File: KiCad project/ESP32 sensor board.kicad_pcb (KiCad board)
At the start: 4 copper layers, 89.5 x 52.8 mm, 85 parts, among them J1 USB_C_Receptacle, J2 JST_2mm_LiPo, J3 GSD090012SEU, J4 B4B-XH-AM, J6 Conn_01x05, Q1 TEMT6000X01, Q2 BC817, Q3 BC817, SW1 1101NE, SW2 1101NE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

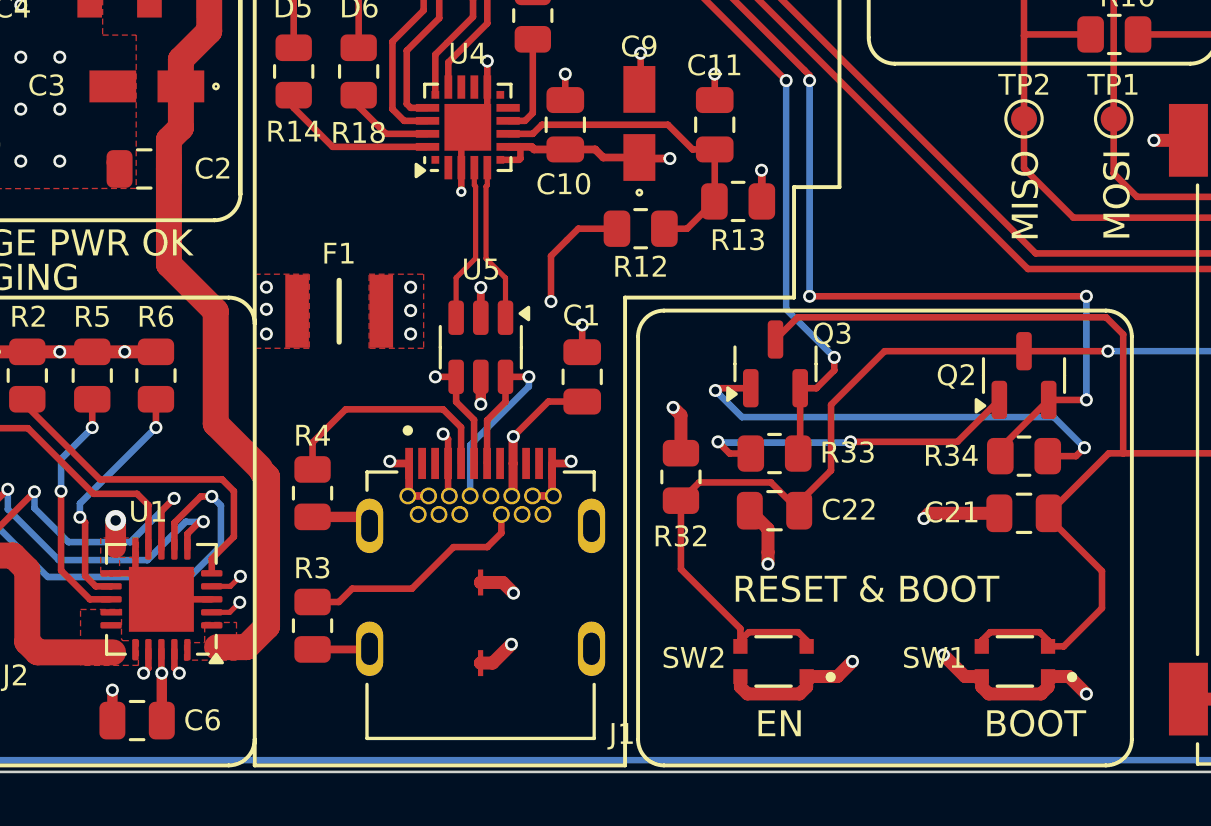
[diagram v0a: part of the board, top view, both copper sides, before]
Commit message: Additional checks completed, and Gerbers exported for HQDFM. Looking good for manufacturing.
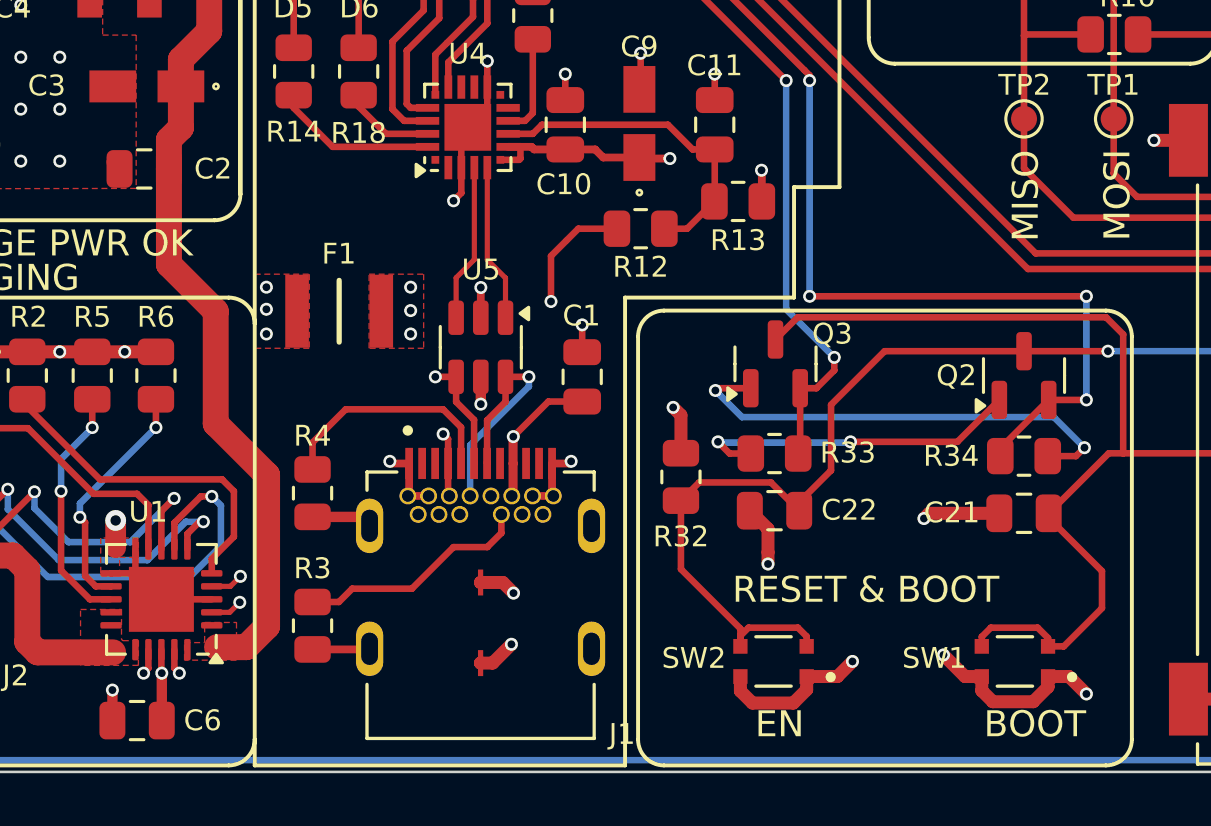
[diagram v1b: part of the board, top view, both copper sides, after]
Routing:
- net GND: track 120.6 -> 121.8 mm

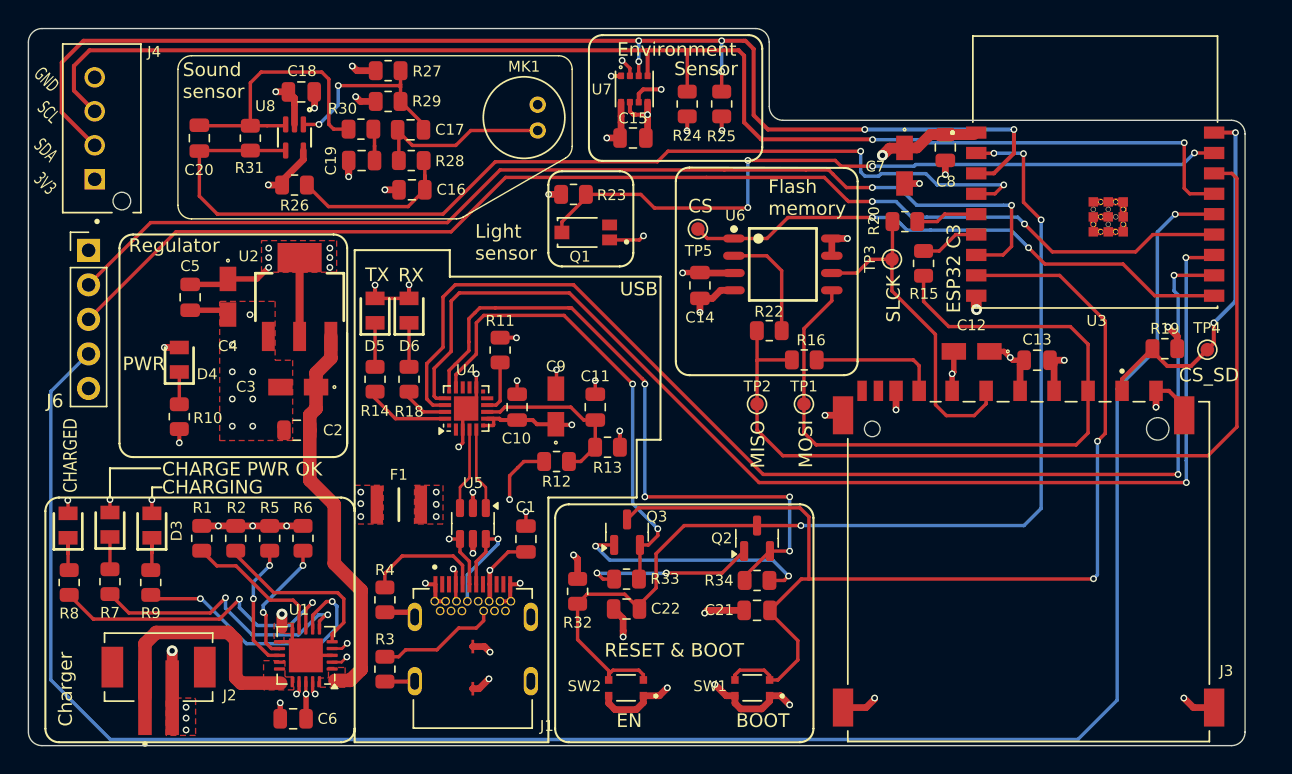
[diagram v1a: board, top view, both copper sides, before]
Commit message: Finished layout update for prototype #2.
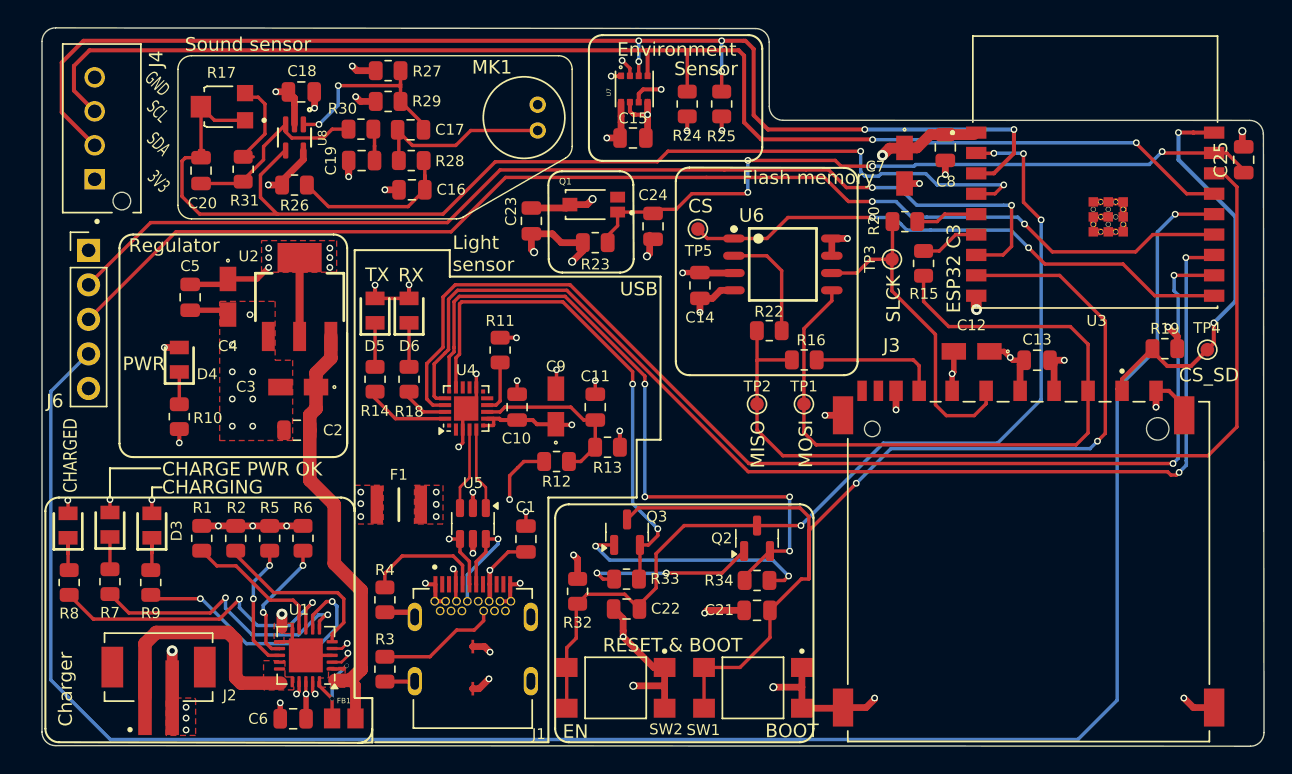
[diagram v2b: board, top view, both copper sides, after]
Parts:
- added C23: 0.1u, Capacitor_SMD:C_0805_2012Metric, F.Cu at (147.5, 86.4)
- added C24: 10n, Capacitor_SMD:C_0805_2012Metric, F.Cu at (156.4, 86.8)
- added C25: 10n, Capacitor_SMD:C_0805_2012Metric, F.Cu at (199.9, 81.9)
- added FB1: FBMJ2125HM330-T, Footprints:BEADC2012X105N, F.Cu at (133.7, 123.0)
- added R17: 35WR100KLFTR, Footprints:TRIM_35WR100KLFTR, F.Cu at (124.8, 78.0)
- C19: value 1u -> 10u
- J3: footprint Project_Library:AMPHENOL_GSD090012SEU -> Footprints:AMPHENOL_GSD090012SEU
- J4: footprint Project_Library:JST_B4B-XH-AM__LF__SN_ -> Footprints:JST_B4B-XH-AM__LF__SN_
- MK1: footprint Project_Library:CUI_CMC-5042PF-AC -> Footprints:CUI_CMC-5042PF-AC
- Q1: footprint Project_Library:TRANS_TEMT6000X01 -> Footprints:TRANS_TEMT6000X01
- R30: value 10K -> 1K
- R31: value 100K -> 22K
- SW1, SW2: footprint Footprints:SW_USLPT2819DT2TR -> Footprints:SW_TL3305AF260QG
- U6: footprint Project_Library:SOIC127P790X216-8N -> Footprints:SOIC127P790X216-8N
- U7: footprint Project_Library:PSON65P250X250X100-8N -> Footprints:PSON65P250X250X100-8N
- U8: footprint Project_Library:SOT65P210X110-5N -> Footprints:SOT65P210X110-5N
- moved R23 3.89 mm to (152.2, 88.0), turned to 180 degrees
- moved C20 2.39 mm to (123.2, 82.7), turned to 90 degrees
- moved R31 2.35 mm to (126.3, 82.6), turned to 90 degrees
- moved Q1 2.13 mm to (152.1, 85.2)
- moved SW2 0.76 mm to (153.7, 120.8), turned to -90 degrees
- moved SW1 0.05 mm to (163.8, 120.8), turned to -90 degrees
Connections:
- Q1 pad 1: GND -> /ESP32-C3-02/PHOTO_C
- Q1 pad 3: /ESP32-C3-02/PHOTO_C -> 3.3V
- R23 pad 1: 3.3V -> /ESP32-C3-02/PHOTO_C
- R23 pad 2: /ESP32-C3-02/PHOTO_C -> GND
- R31 pad 2: /ESP32-C3-02/MIC_OUT -> Net-(R17-Pad3)
- SW1 pad 2: GND -> /ESP32-C3-02/BOOT
- SW1 pad 3: /ESP32-C3-02/BOOT -> GND
- SW2 pad 2: GND -> /ESP32-C3-02/EN
- SW2 pad 3: /ESP32-C3-02/EN -> GND
- U1 pad 1: +5V -> Net-(FB1-Pad2)
- U1 pad 20: +5V -> Net-(FB1-Pad2)
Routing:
- net GND: track 121.8 -> 132.7 mm, vias 53 -> 55
- net /ESP32-C3-02/MIC_OUT: track 75.7 -> 85.1 mm
- net Net-(FB1-Pad2): track 0.00 -> 7.13 mm, vias 0 -> 2
- net Net-(R17-Pad3): track 0.00 -> 6.88 mm
- net /ESP32-C3-02/EN: track 80.2 -> 73.4 mm
- net Net-(U8-IN-): track 20.8 -> 14.4 mm
- net 3.3V: track 67.6 -> 71.4 mm
- net /ESP32-C3-02/BOOT: track 84.3 -> 80.8 mm
- net +5V: track 29.0 -> 31.9 mm
- net /ESP32-C3-02/DTS: track 35.2 -> 38.1 mm
- net /ESP32-C3-02/CS_SD: track 27.6 -> 30.4 mm
- net /ESP32-C3-02/RTS: track 49.0 -> 51.3 mm
- net /ESP32-C3-02/SCL: track 102.5 -> 100.6 mm
- net /ESP32-C3-02/TX_RX: track 87.5 -> 86.1 mm
- net /ESP32-C3-02/PHOTO_C: track 53.8 -> 52.9 mm
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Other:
- board size 89.5 x 52.8 mm -> 89.9 x 52.8 mm

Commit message: Swapped pins for CS_SD and MIC_OUT so that the microphone is connected to a usable ADC.
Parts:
- C20: value 0.1u -> 100p
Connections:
- U3 pad 18: /ESP32-C3-02/CS_SD -> /ESP32-C3-02/MIC_OUT
- U3 pad 4: /ESP32-C3-02/MIC_OUT -> /ESP32-C3-02/CS_SD
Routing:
- net /ESP32-C3-02/MIC_OUT: track 85.1 -> 99.9 mm
- net /ESP32-C3-02/BOOT: track 80.8 -> 79.6 mm
- net /ESP32-C3-02/EN: track 73.4 -> 74.3 mm
- net /ESP32-C3-02/CS_SD: track 30.4 -> 29.8 mm, vias 2 -> 0
